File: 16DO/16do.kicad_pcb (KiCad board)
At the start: 2 copper layers, 109 x 100 mm, 66 parts, among them J1 Conn_02x10_Counter_Clockwise, J2 Conn_02x36_Counter_Clockwise, J3 Conn_02x36_Counter_Clockwise, P1 CONN_01X08, P2 CONN_01X08, U1 STM32F373V8Tx, U10 SP3485, U2 ULN2803A, U3 ULN2803A, U4 LD3985G33R_TSOT23, U5 AP1117-33, U6 SP3485, U7 SP3485, U8 SI8621, U9 SP3485, Y1 Crystal_GND3

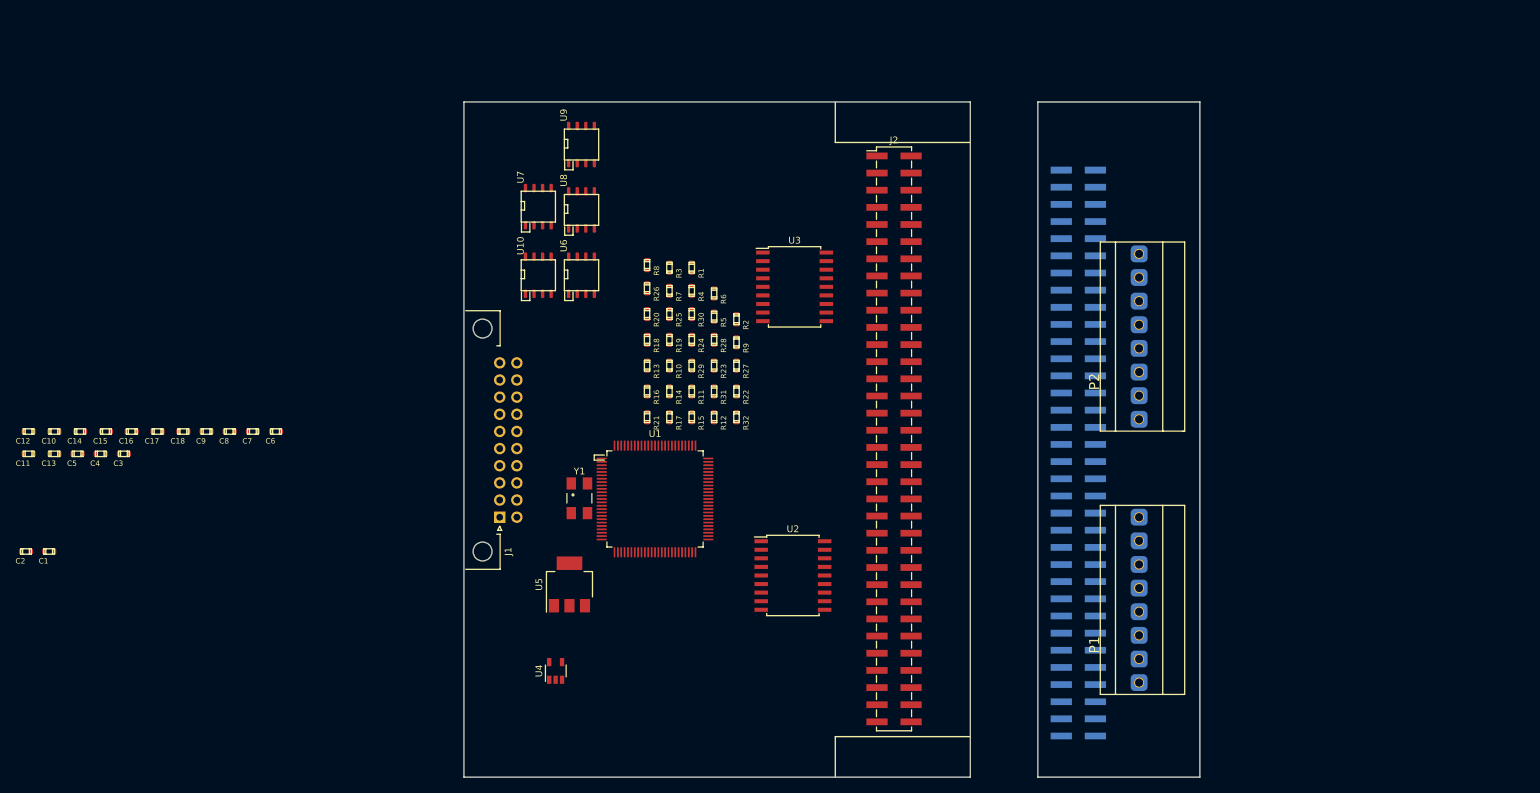
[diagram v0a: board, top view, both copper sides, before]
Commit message: add dual color leds, finalize formfactor
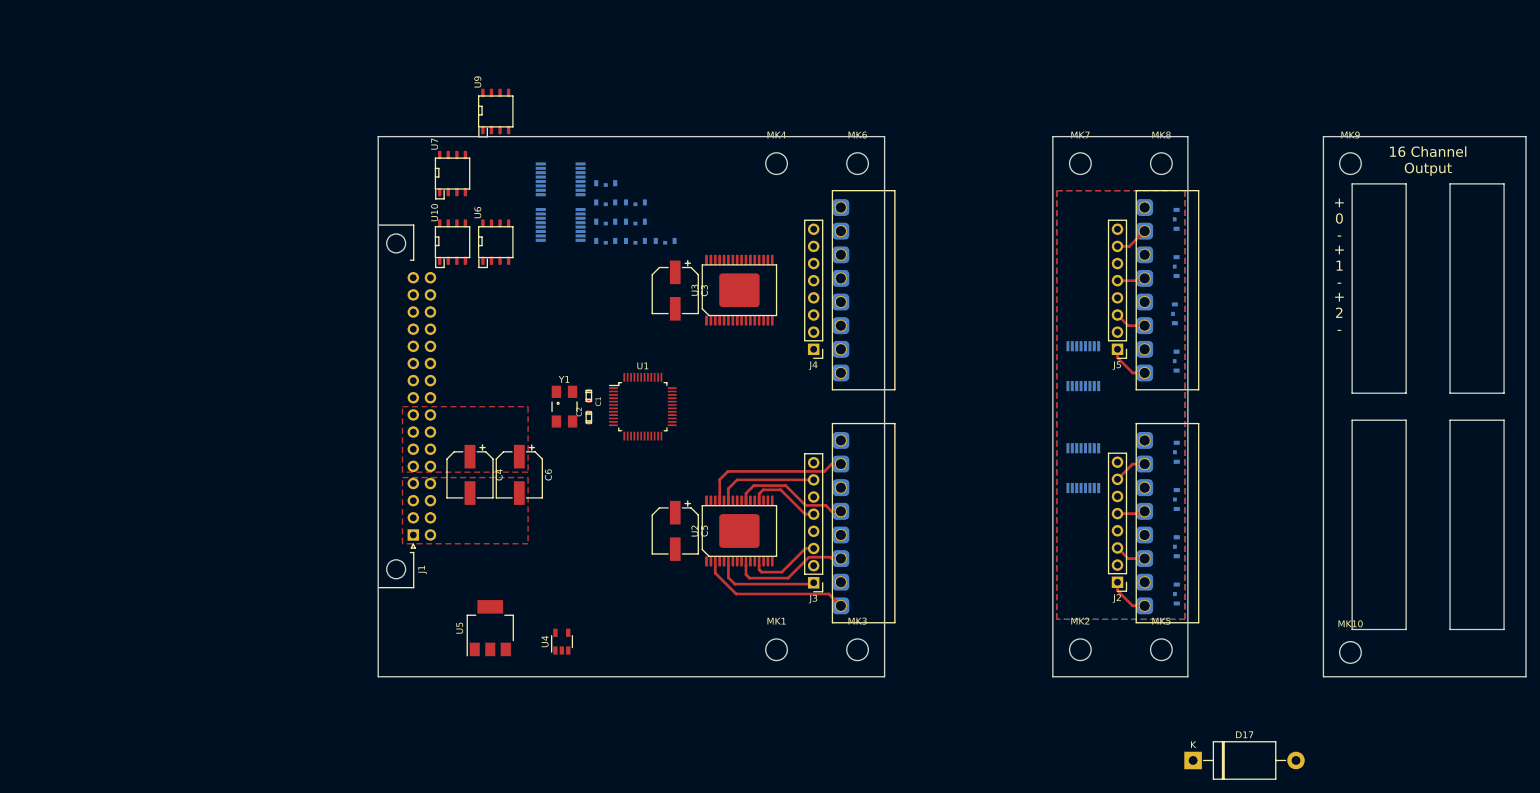
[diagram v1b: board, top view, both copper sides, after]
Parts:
- removed C10, C11, C12, C13, C14, C15, C16, C17, C18, C7, C8, C9: C, stmbl-kicad-lib:C_0603
- removed R1, R10, R11, R12, R13, R14, R15, R16, R17, R18, R19, R2, R20, R21, R22, R23, R24, R25, R26, R27, R28, R29, R3, R30, R31, R32, R4, R5, R6, R7, R8, R9: R, stmbl-kicad-lib:C_0603
- removed U8: SI8621, stmbl-kicad-lib:SOIC-8-N
- added D1: LED_Dual_CCA, stmbl:LED1206Duo-SIDE, B.Cu at (194.4, 117.8)
- added D10: LED_Dual_CCA, stmbl:LED1206Duo-SIDE, B.Cu at (114.2, 65.5)
- added D11: LED_Dual_CCA, stmbl:LED1206Duo-SIDE, B.Cu at (109.8, 62.6)
- added D12: LED_Dual_CCA, stmbl:LED1206Duo-SIDE, B.Cu at (109.8, 59.8)
- added D13: LED_Dual_CCA, stmbl:LED1206Duo-SIDE, B.Cu at (114.2, 62.6)
- added D14: LED_Dual_CCA, stmbl:LED1206Duo-SIDE, B.Cu at (118.6, 65.5)
- added D15: LED_Dual_CCA, stmbl:LED1206Duo-SIDE, B.Cu at (109.8, 56.9)
- added D16: LED_Dual_CCA, stmbl:LED1206Duo-SIDE, B.Cu at (114.2, 59.8)
- added D17: 1.5KExxA, Diode_THT:D_DO-201AE_P15.24mm_Horizontal, F.Cu at (196.8, 142.4)
- added D2: LED_Dual_CCA, stmbl:LED1206Duo-SIDE, B.Cu at (194.4, 110.8)
- added D3: LED_Dual_CCA, stmbl:LED1206Duo-SIDE, B.Cu at (194.4, 103.8)
- added D4: LED_Dual_CCA, stmbl:LED1206Duo-SIDE, B.Cu at (194.4, 96.8)
- added D5: LED_Dual_CCA, stmbl:LED1206Duo-SIDE, B.Cu at (194.3, 83.2)
- added D6: LED_Dual_CCA, stmbl:LED1206Duo-SIDE, B.Cu at (194.1, 76.2)
- added D7: LED_Dual_CCA, stmbl:LED1206Duo-SIDE, B.Cu at (194.3, 69.2)
- added D8: LED_Dual_CCA, stmbl:LED1206Duo-SIDE, B.Cu at (194.3, 62.2)
- added D9: LED_Dual_CCA, stmbl:LED1206Duo-SIDE, B.Cu at (109.8, 65.5)
- added J4: CONN_01X16, Connector_PinHeader_2.54mm:PinHeader_1x08_P2.54mm_Vertical, F.Cu at (140.6, 81.5)
- added J5: CONN_01X16, Connector_PinHeader_2.54mm:PinHeader_1x08_P2.54mm_Vertical, F.Cu at (185.6, 81.5)
- added MK1: Mounting_Hole, MountingHole:MountingHole_3.2mm_M3, F.Cu at (135.1, 126.0)
- added MK10: Mounting_Hole, MountingHole:MountingHole_3.2mm_M3, F.Cu at (220.1, 126.4)
- added MK2: Mounting_Hole, MountingHole:MountingHole_3.2mm_M3, F.Cu at (180.1, 126.0)
- added MK3: Mounting_Hole, MountingHole:MountingHole_3.2mm_M3, F.Cu at (147.1, 126.0)
- added MK4: Mounting_Hole, MountingHole:MountingHole_3.2mm_M3, F.Cu at (135.1, 54.0)
- added MK5: Mounting_Hole, MountingHole:MountingHole_3.2mm_M3, F.Cu at (192.1, 126.0)
- added MK6: Mounting_Hole, MountingHole:MountingHole_3.2mm_M3, F.Cu at (147.1, 54.0)
- added MK7: Mounting_Hole, MountingHole:MountingHole_3.2mm_M3, F.Cu at (180.1, 54.0)
- added MK8: Mounting_Hole, MountingHole:MountingHole_3.2mm_M3, F.Cu at (192.1, 54.0)
- added MK9: Mounting_Hole, MountingHole:MountingHole_3.2mm_M3, F.Cu at (220.1, 54.0)
- added P3: CONN_01X08, stmbl:RM3.5_1x8, F.Cu at (189.6, 85.0)
- added P4: CONN_01X08, stmbl:RM3.5_1x8, F.Cu at (189.6, 119.5)
- added U13: 74HC595, Package_SO:TSSOP-16_4.4x5mm_P0.65mm, B.Cu at (180.5, 99.1)
- added U14: 74HC595, Package_SO:TSSOP-16_4.4x5mm_P0.65mm, B.Cu at (180.5, 84.0)
- added U15: 74HC595, Package_SO:TSSOP-16_4.4x5mm_P0.65mm, B.Cu at (103.1, 63.1)
- added U16: 74HC595, Package_SO:TSSOP-16_4.4x5mm_P0.65mm, B.Cu at (103.1, 56.3)
- C1, C2: footprint stmbl-kicad-lib:C_0603 -> stmbl:C_0603
- C3, C4, C5, C6: value C -> 100µ; footprint stmbl-kicad-lib:C_0603 -> Capacitor_SMD:CP_Elec_6.3x7.7
- J1: value Conn_02x10_Counter_Clockwise -> Conn_02x16_Row_Letter_First; footprint Connectors_IEC_DIN:Conn_DIN41612_3B020M -> Connector_DIN:DIN41612_B2_2x16_Horizontal
- J2: value Conn_02x36_Counter_Clockwise -> CONN_01X16; footprint Pin_Headers:Pin_Header_Straight_2x34_Pitch2.54mm_SMD -> Connector_PinHeader_2.54mm:PinHeader_1x08_P2.54mm_Vertical
- J3: value Conn_02x36_Counter_Clockwise -> CONN_01X16; footprint Pin_Headers:Pin_Header_Straight_2x34_Pitch2.54mm_SMD -> Connector_PinHeader_2.54mm:PinHeader_1x08_P2.54mm_Vertical; moved to F.Cu
- P1, P2: footprint stmbl-kicad-lib:PW06308VBEC -> stmbl:RM3.5_1x8
- U1: value STM32F373V8Tx -> STM32F030CCTx; footprint stmbl-kicad-lib:LQFP-100_14x14mm_Pitch0.5mm -> Package_QFP:LQFP-48_7x7mm_P0.5mm
- U2, U3: value ULN2803A -> MC33879A; footprint Housings_SOIC:SOIC-18W_7.5x11.6mm_Pitch1.27mm -> stmbl:SOICW_32_EPAD
- moved C5 89.3 mm to (120.1, 108.4), turned to 270 degrees
- moved C2 85.7 mm to (107.3, 91.6), turned to 270 degrees
- moved C3 85.2 mm to (120.1, 72.8), turned to 270 degrees
- moved C1 83.2 mm to (107.3, 88.4), turned to 90 degrees
- moved C4 54.8 mm to (89.7, 100.1), turned to 270 degrees
- moved P1 45.6 mm to (144.6, 119.5)
- moved P2 44.7 mm to (144.6, 85.0)
- moved J3 43.7 mm to (140.6, 116.1), turned to 180 degrees
- moved J2 39.3 mm to (185.6, 116.0), turned to 180 degrees
- moved C6 36.6 mm to (97.0, 100.1), turned to 270 degrees
- moved U1 13.8 mm to (115.3, 90.0)
- moved Y1 13.7 mm to (103.7, 90.0)
- moved U10 13.6 mm to (87.1, 65.6)
- moved U7 13.6 mm to (87.1, 55.5)
- moved U6 13.6 mm to (93.5, 65.6)
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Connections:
- net SDADC1_AIN0 renamed Net-(U1-Pad43)
- net SDADC1_AIN1 renamed Net-(U1-Pad42)
- net SDADC1_AIN2 renamed Net-(U1-Pad41)
- net SDADC1_AIN3 renamed Net-(U1-Pad38)
- net SDADC1_AIN4 renamed Net-(U1-Pad37)
- net SDADC1_AIN7 renamed Net-(U1-Pad40)
- net SDADC1_AIN8 renamed Net-(U1-Pad39)
- net SDADC2_AIN0 renamed Net-(U1-Pad46)
- net SDADC2_AIN1 renamed Net-(U1-Pad45)
- net SDADC2_AIN2 renamed Net-(U1-Pad44)
- C3 pad 1: ADC0 -> +24V
- C3 pad 2: GND -> GNDPWR
- C4 pad 1: ADC8 -> +24V
- C4 pad 2: GND -> GNDPWR
- C5 pad 1: ADC1 -> +24V
- C5 pad 2: GND -> GNDPWR
- C6 pad 1: ADC9 -> +24V
- C6 pad 2: GND -> GNDPWR
- J2 pad 1: OUT8 -> OUT12
- J2 pad 2: Net-(J2-Pad2) -> GNDPWR
- J2 pad 3: OUT8 -> OUT13
- J2 pad 4: Net-(J2-Pad4) -> GNDPWR
- J2 pad 5: OUT9 -> OUT14
- J2 pad 6: Net-(J2-Pad6) -> GNDPWR
- J2 pad 7: OUT9 -> OUT15
- J2 pad 8: Net-(J2-Pad8) -> GNDPWR
- J3 pad 1: COUT0 -> OUT12
- J3 pad 2: Net-(J3-Pad2) -> GNDPWR
- J3 pad 3: COUT0 -> OUT13
- J3 pad 4: Net-(J3-Pad4) -> GNDPWR
- J3 pad 5: COUT1 -> OUT14
- J3 pad 6: Net-(J3-Pad6) -> GNDPWR
- J3 pad 7: COUT1 -> OUT15
- J3 pad 8: Net-(J3-Pad8) -> GNDPWR
- P1 pad 1: COUT0 -> OUT0
- P1 pad 2: COUT1 -> GNDPWR
- P1 pad 3: COUT2 -> OUT1
- P1 pad 4: COUT3 -> GNDPWR
- P1 pad 5: COUT4 -> OUT2
- P1 pad 6: COUT5 -> GNDPWR
- P1 pad 7: COUT6 -> OUT3
- P1 pad 8: COUT7 -> GNDPWR
- P2 pad 1: COUT8 -> OUT4
- P2 pad 2: COUT9 -> GNDPWR
- P2 pad 3: COUT10 -> OUT5
- P2 pad 4: COUT11 -> GNDPWR
- P2 pad 5: COUT12 -> OUT6
- P2 pad 6: COUT13 -> GNDPWR
- P2 pad 7: COUT14 -> OUT7
- P2 pad 8: COUT15 -> GNDPWR
- U1 pad 12: Net-(C1-Pad1) -> Net-(U1-Pad12)
- U1 pad 13: Net-(C2-Pad1) -> Net-(U1-Pad13)
- U1 pad 15: ADC10 -> Net-(U1-Pad15)
- U1 pad 16: ADC11 -> Net-(U1-Pad16)
- U1 pad 17: ADC12 -> Net-(U1-Pad17)
- U1 pad 18: ADC13 -> Net-(U1-Pad18)
- U1 pad 23: ADC0 -> Net-(U1-Pad23)
- U1 pad 24: ADC1 -> Net-(U1-Pad24)
- U1 pad 25: ADC2 -> Net-(U1-Pad25)
- U1 pad 26: ADC3 -> Net-(U1-Pad26)
- U1 pad 29: ADC4 -> Net-(U1-Pad29)
- U1 pad 30: ADC5 -> Net-(U1-Pad30)
- U1 pad 31: ADC6 -> Net-(U1-Pad31)
- U1 pad 32: ADC7 -> Net-(U1-Pad32)
- U1 pad 33: ADC14 -> Net-(U1-Pad33)
- U1 pad 34: ADC15 -> Net-(U1-Pad34)
- U1 pad 35: ADC8 -> Net-(U1-Pad35)
- U1 pad 36: ADC9 -> Net-(U1-Pad36)
- U1 pad 47: OD8 -> Net-(U1-Pad47)
- U1 pad 5: Net-(U1-Pad5) -> Net-(C1-Pad1)
- U1 pad 6: Net-(U1-Pad6) -> Net-(C2-Pad1)
- U2 pad 1: OD0 -> GNDPWR
- U2 pad 10: GND -> OUT1
- U2 pad 11: OUT7 -> +24V
- U2 pad 12: OUT6 -> +24V
- U2 pad 13: OUT5 -> OUT13
- U2 pad 14: OUT4 -> PWM3
- U2 pad 15: OUT3 -> EN_OUT
- U2 pad 16: OUT2 -> SPI_CLK
- U2 pad 17: OUT1 -> Net-(U2-Pad17)
- U2 pad 18: OUT0 -> SPI_MISO
- U2 pad 2: OD1 -> Net-(U2-Pad2)
- U2 pad 3: OD2 -> OUT0
- U2 pad 4: OD3 -> Net-(U2-Pad4)
- U2 pad 5: OD4 -> +24V
- U2 pad 6: OD5 -> OUT12
- U2 pad 7: OD6 -> +24V
- U2 pad 8: OD7 -> Net-(U2-Pad8)
- U2 pad 9: GND -> Net-(U2-Pad9)
- U3 pad 1: OD8 -> GNDPWR
- U3 pad 10: GND -> OUT8
- U3 pad 11: OUT15 -> +24V
- U3 pad 12: OUT14 -> +24V
- U3 pad 13: OUT13 -> OUT5
- U3 pad 14: OUT12 -> PWM1
- U3 pad 15: OUT11 -> EN_OUT
- U3 pad 16: OUT10 -> SPI_CLK
- U3 pad 17: OUT9 -> SPI_MOSI
- U3 pad 18: OUT8 -> SPI_MISO
- U3 pad 2: OD9 -> Net-(U3-Pad2)
- U3 pad 3: OD10 -> OUT7
- U3 pad 4: OD11 -> Net-(U3-Pad4)
- U3 pad 5: OD12 -> +24V
- U3 pad 6: OD13 -> OUT9
- U3 pad 7: OD14 -> +24V
- U3 pad 8: OD15 -> Net-(U3-Pad8)
- U3 pad 9: GND -> Net-(U3-Pad9)
- Y1 pad 3: Net-(C1-Pad2) -> (no net)
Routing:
- net OUT3: track 0.00 -> 22.6 mm
- net OUT0: track 0.00 -> 21.8 mm
- net OUT12: track 0.00 -> 21.1 mm
- net OUT15: track 0.00 -> 20.5 mm
- net OUT2: track 0.00 -> 17.8 mm
- net OUT1: track 0.00 -> 17.0 mm
- net OUT14: track 0.00 -> 15.6 mm
- net OUT13: track 0.00 -> 15.0 mm
- net OUT8: track 0.00 -> 6.21 mm
- net OUT11: track 0.00 -> 4.96 mm
- net OUT9: track 0.00 -> 4.68 mm
- net OUT10: track 0.00 -> 4.16 mm
- added copper zone on F.Cu, net +24V
- added copper zone on B.Cu, net GNDPWR
- added copper zone on F.Cu, net GNDPWR
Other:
- board size 109 x 100 mm -> 170 x 80 mm
- net class Default: clearance 0.2 -> 0.15
- rule trace_clearance: 0.2 -> 0.15
- rule trace_min: 0.2 -> 0.15
- board text added: "+ 0 -"
- board text added: "+ 1 -"
- board text added: "+ 2 -"
- board text added: "16 Channel Output"
- board text added: "STMBL 16DO V0.1 Frontplate"
- board text added: "STMBL 16xx riser V0.1 dualcolor LED"

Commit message: add diff spi, rs485, started routing
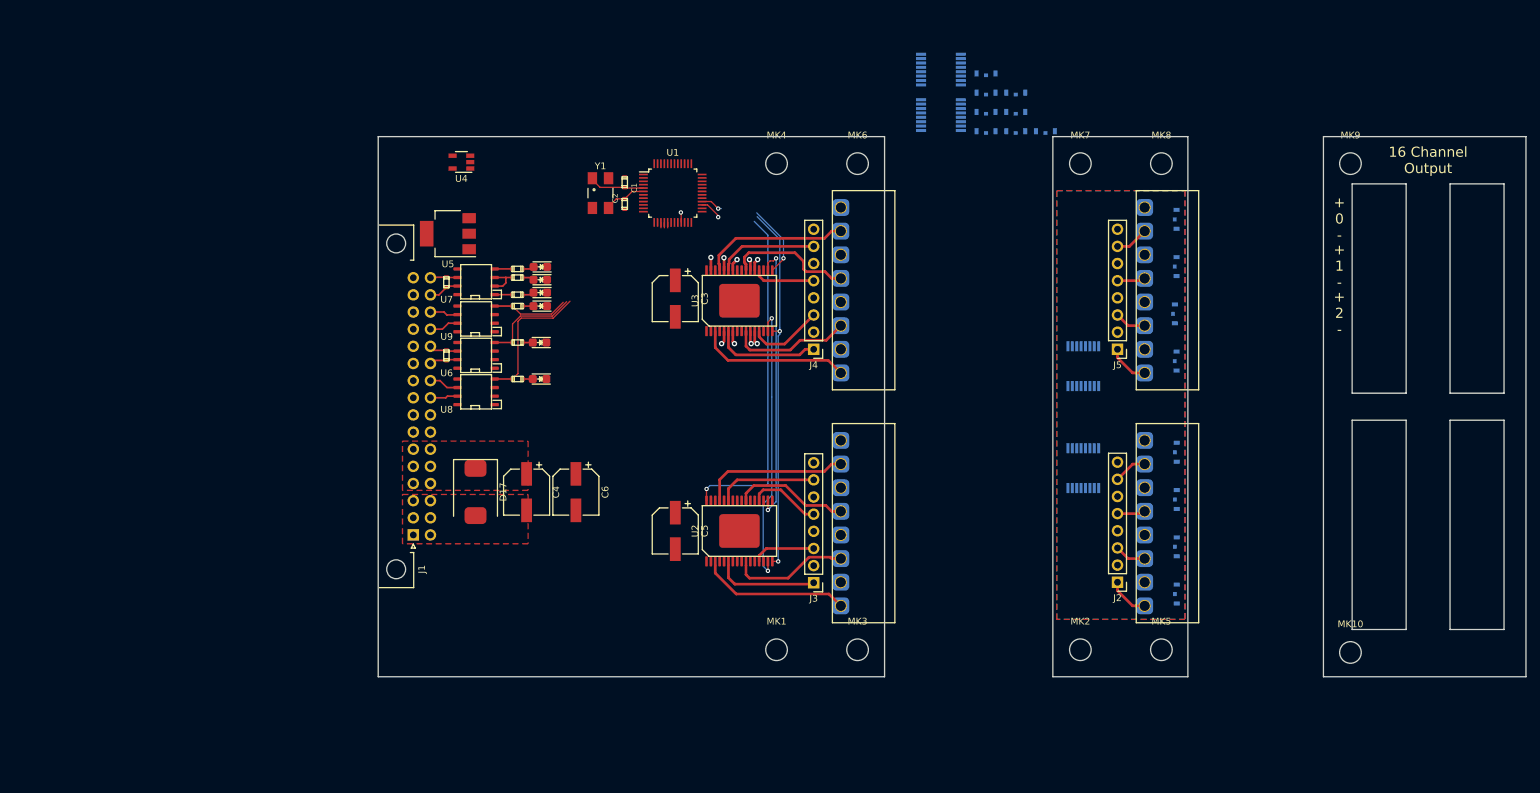
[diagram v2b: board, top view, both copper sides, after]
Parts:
- removed U10: SP3485, stmbl-kicad-lib:SOIC-8-N
- added D18: LED, stmbl:LED-0805, F.Cu at (100.0, 80.5)
- added D19: LED, stmbl:LED-0805, F.Cu at (100.0, 85.9)
- added D20: LED, stmbl:LED-0805, F.Cu at (100.1, 75.1)
- added D21: LED, stmbl:LED-0805, F.Cu at (100.1, 73.1)
- added D22: LED, stmbl:LED-0805, F.Cu at (100.1, 69.3)
- added D23: LED, stmbl:LED-0805, F.Cu at (100.1, 71.2)
- added R1: R, stmbl:R_0603, F.Cu at (86.2, 82.4)
- added R2: R, stmbl:R_0603, F.Cu at (86.2, 71.6)
- added R3: R, stmbl:R_0603, F.Cu at (96.7, 80.5)
- added R4: R, stmbl:R_0603, F.Cu at (96.7, 85.9)
- added R5: R, stmbl:R_0603, F.Cu at (96.7, 75.1)
- added R6: R, stmbl:R_0603, F.Cu at (96.7, 73.4)
- added R7: R, stmbl:R_0603, F.Cu at (96.7, 69.6)
- added R8: R, stmbl:R_0603, F.Cu at (96.7, 70.9)
- added U8: SP3485, stmbl:SOIC-8-N, F.Cu at (90.6, 87.8)
- D17: footprint Diode_THT:D_DO-201AE_P15.24mm_Horizontal -> stmbl:D_SMC
- U6, U7, U9: footprint stmbl-kicad-lib:SOIC-8-N -> stmbl:SOIC-8-N
- moved D17 113.5 mm to (90.5, 102.6), turned to 270 degrees
- moved U4 72.6 mm to (88.4, 53.8), turned to 180 degrees
- moved U5 58.8 mm to (86.4, 64.4), turned to 180 degrees
- moved D10 58.6 mm to (170.5, 49.2)
- moved D13 58.6 mm to (170.5, 46.3)
- moved D16 58.6 mm to (170.5, 43.5)
- moved D11 58.6 mm to (166.1, 46.3)
- moved D12 58.6 mm to (166.1, 43.5)
- moved D14 58.6 mm to (174.9, 49.2)
- moved D15 58.6 mm to (166.1, 40.6)
- moved D9 58.6 mm to (166.1, 49.2)
- moved U15 58.6 mm to (159.4, 46.8)
- moved U16 58.6 mm to (159.4, 40.1)
- moved Y1 32.1 mm to (109.0, 58.4)
- moved C1 32.1 mm to (112.6, 56.8)
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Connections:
- net Net-(U1-Pad10) renamed AIN0
- net Net-(U1-Pad11) renamed AIN1
- net Net-(U1-Pad12) renamed AIN2
- net Net-(U1-Pad13) renamed AIN3
- J1 pad a4: GNDPWR -> +24V
- J1 pad a7: +24V -> +12V
- J1 pad a8: +24V -> Net-(J1-Pada8)
- J1 pad b10: Net-(J1-Padb10) -> DSPI_MOSI_A
- J1 pad b11: Net-(J1-Padb11) -> DSPI_MISO_B
- J1 pad b12: Net-(J1-Padb12) -> DSPI_MISO_A
- J1 pad b13: Net-(J1-Padb13) -> DSPI_SCK_B
- J1 pad b14: Net-(J1-Padb14) -> DSPI_SCK_A
- J1 pad b15: Net-(J1-Padb15) -> USART1_B
- J1 pad b16: Net-(J1-Padb16) -> USART1_A
- J1 pad b4: GNDPWR -> +24V
- J1 pad b7: +24V -> +12V
- J1 pad b8: +24V -> Net-(J1-Padb8)
- J1 pad b9: Net-(J1-Padb9) -> DSPI_MOSI_B
- U1 pad 15: Net-(U1-Pad15) -> DSPI_SCK
- U1 pad 16: Net-(U1-Pad16) -> DSPI_MISO
- U1 pad 17: Net-(U1-Pad17) -> DSPI_MOSI
- U1 pad 21: Net-(U1-Pad21) -> SPI_SCK
- U1 pad 27: Net-(U1-Pad27) -> SPI_MISO
- U1 pad 28: Net-(U1-Pad28) -> SPI_MOSI
- U1 pad 29: Net-(U1-Pad29) -> PWM0
- U1 pad 30: Net-(U1-Pad30) -> PWM1
- U1 pad 31: Net-(U1-Pad31) -> PWM2
- U1 pad 32: Net-(U1-Pad32) -> PWM3
- U1 pad 33: Net-(U1-Pad33) -> USART1_EN
- U1 pad 4: Net-(U1-Pad4) -> EN_OUT
- U1 pad 42: Net-(U1-Pad42) -> USART1_TX
- U1 pad 43: Net-(U1-Pad43) -> USART1_RX
- U2 pad 16: SPI_CLK -> SPI_SCK
- U2 pad 18: SPI_MISO -> SPI_CS_OUT
- U2 pad 32: Net-(U2-Pad32) -> SPI_MISO
- U3 pad 10: OUT8 -> OUT5
- U3 pad 13: OUT5 -> OUT9
- U3 pad 16: SPI_CLK -> SPI_SCK
- U3 pad 18: SPI_MISO -> SPI_CS_OUT
- U3 pad 20: OUT4 -> OUT10
- U3 pad 23: OUT10 -> OUT6
- U3 pad 29: OUT6 -> OUT7
- U3 pad 3: OUT7 -> OUT4
- U3 pad 6: OUT9 -> OUT8
- U6 pad 2: Net-(U6-Pad2) -> +3V3
- U6 pad 3: Net-(U6-Pad3) -> GNDD
- U6 pad 4: Net-(U6-Pad4) -> DSPI_MISO
- U6 pad 6: Net-(U6-Pad6) -> DSPI_MISO_A
- U6 pad 7: Net-(U6-Pad7) -> DSPI_MISO_B
- U7 pad 1: Net-(U7-Pad1) -> USART1_RX
- U7 pad 2: Net-(U7-Pad2) -> USART1_EN
- U7 pad 3: Net-(U7-Pad3) -> USART1_EN
- U7 pad 4: Net-(U7-Pad4) -> USART1_TX
- U7 pad 6: Net-(U7-Pad6) -> USART1_A
- U7 pad 7: Net-(U7-Pad7) -> USART1_B
- U9 pad 2: Net-(U9-Pad2) -> GNDD
- U9 pad 3: Net-(U9-Pad3) -> +3V3
- U9 pad 4: Net-(U9-Pad4) -> DSPI_SCK
- U9 pad 6: Net-(U9-Pad6) -> DSPI_SCK_A
- U9 pad 7: Net-(U9-Pad7) -> DSPI_SCK_B
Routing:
- net SPI_SCK: track 0.00 -> 56.0 mm, vias 0 -> 3
- net SPI_MISO: track 0.00 -> 54.1 mm, vias 0 -> 2
- net EN_OUT: track 0.00 -> 41.8 mm, vias 0 -> 2
- net SPI_CS_OUT: track 0.00 -> 41.8 mm, vias 0 -> 2
- net OUT4: track 0.00 -> 22.6 mm
- net OUT7: track 0.00 -> 21.8 mm
- net DSPI_MOSI: track 0.00 -> 21.3 mm
- net OUT6: track 0.00 -> 18.9 mm
- net OUT5: track 0.00 -> 18.0 mm
- net +24V: track 0.00 -> 16.9 mm, vias 0 -> 9
- net OUT8: track 6.21 -> 22.0 mm
- net DSPI_MISO: track 0.00 -> 15.6 mm
- net OUT11: track 4.96 -> 20.0 mm
- net SPI_MOSI: track 0.00 -> 14.1 mm, vias 0 -> 2
- net DSPI_SCK: track 0.00 -> 12.2 mm
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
